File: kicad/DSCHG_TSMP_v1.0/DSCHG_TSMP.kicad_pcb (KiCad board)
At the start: 2 copper layers, 100 x 50 mm, 22 parts, among them J1 TSMP-, J10 R+, J11 R-, J12 Relay_GND, J13 TSAL_TS-, J14 TSAL_TS+, J2 Dis_Relay-, J3 TSMP+, J4 energy meter+, J5 Dis_Relay+, J6 HV-, J7 HV+, J8 SDC+, J9 SDC+&Relay_GND

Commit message: Add files via upload
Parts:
- removed F1: Fuse, Fuse:Fuse_Littelfuse-NANO2-885
- removed J4: energy meter+, Connector_Molex:Molex_Micro-Fit_3.0_43650-0215_1x02_P3.00mm_Vertical
- moved G*** 27.2 mm to (204.5, 96.5)
- moved J2 26.5 mm to (183.0, 77.0)
- moved J3 22.8 mm to (207.0, 77.0), turned to 0 degrees
- moved R1 16.0 mm to (181.0, 90.0), turned to 0 degrees
- moved R2 12.3 mm to (180.9, 99.0)
- moved J9 3.92 mm to (231.0, 77.1)
- moved J8 3.58 mm to (234.0, 113.0)
- moved J13 2.00 mm to (171.0, 77.0)
- moved J5 2.00 mm to (210.0, 112.9)
- moved J6 2.00 mm to (158.0, 90.0)
- moved J7 2.00 mm to (158.0, 102.0)
- moved J10 2.00 mm to (186.0, 112.9)
- moved J11 2.00 mm to (198.0, 112.9)
- moved J14 2.00 mm to (174.0, 112.9)
- moved J1 2.00 mm to (195.0, 77.0)
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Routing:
- net Net-(J13-Pin_1): track 177.7 -> 120.4 mm
- net Net-(J3-Pin_1): track 36.0 -> 87.3 mm
- net Net-(J4-Pin_1): track 36.5 -> 0.00 mm
- net Net-(J1-Pin_1): track 10.9 -> 46.5 mm
- net Net-(J8-Pin_1): track 62.8 -> 77.8 mm
- net Net-(J10-Pin_1): track 125.4 -> 119.1 mm
- net Net-(J12-Pin_1): track 47.5 -> 46.7 mm
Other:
- outline, holes or cut-outs redrawn
- board text removed: "Energy meter+"

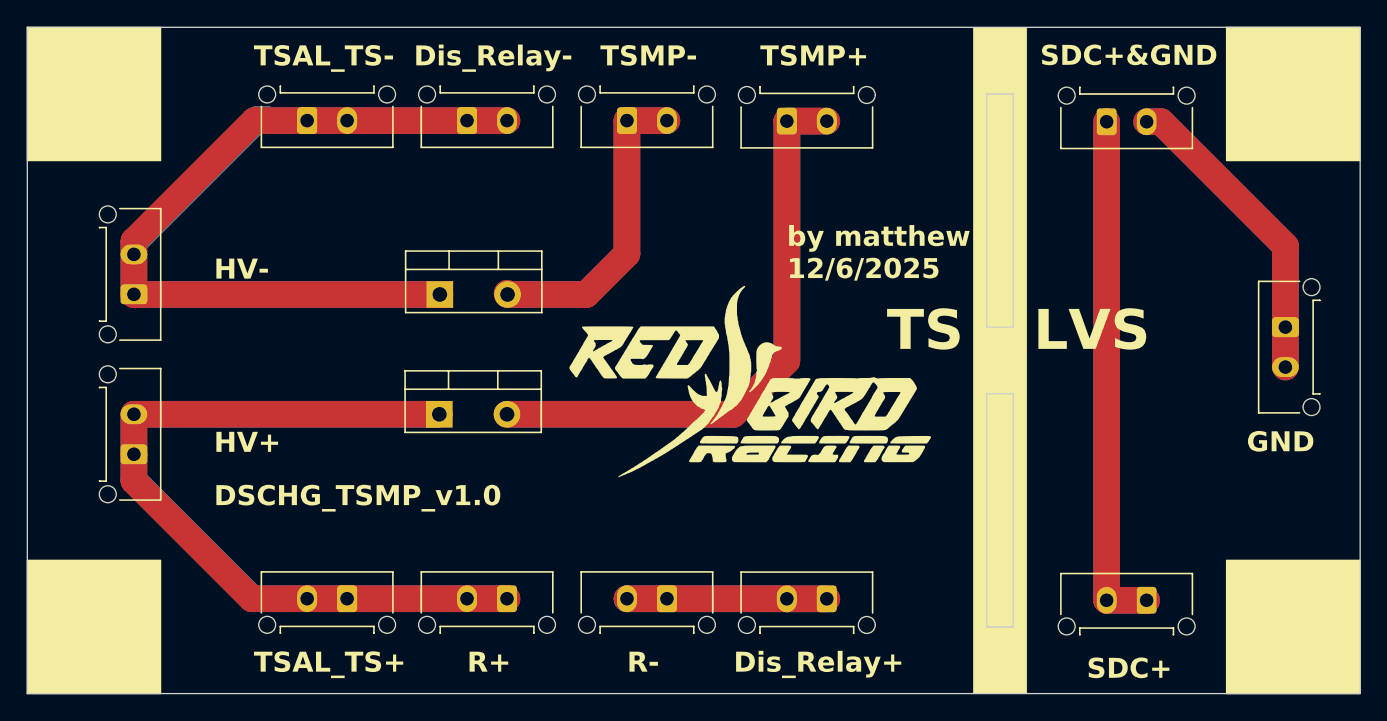
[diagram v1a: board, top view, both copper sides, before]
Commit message: changed some silkscreen
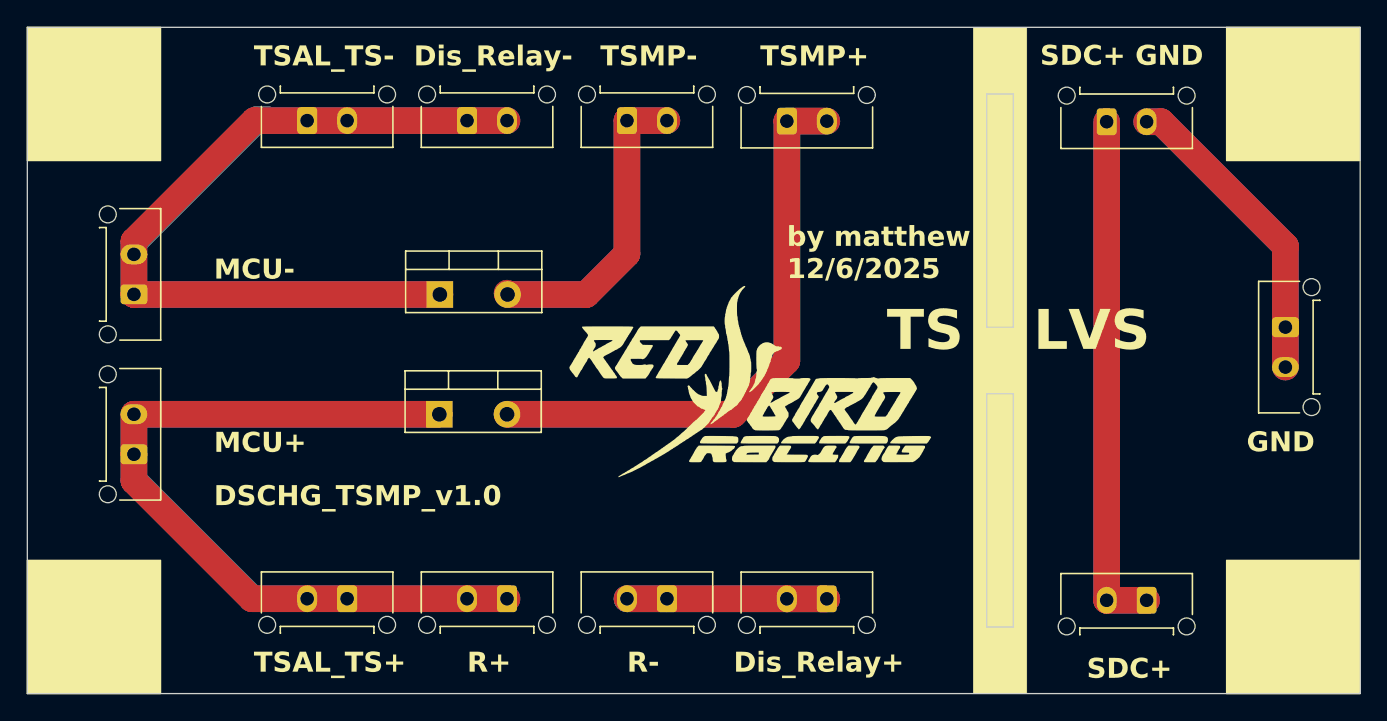
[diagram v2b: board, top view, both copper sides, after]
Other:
- board text added: "MCU+"
- board text added: "MCU-"
- board text added: "SDC+ GND"
- board text removed: "HV+"
- board text removed: "HV-"
- board text removed: "SDC+&GND"
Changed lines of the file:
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@@
 		)
 	)
-	(gr_text "HV+"
+	(gr_text "MCU+\n"
 		(at 164 102.04 0)
 		(layer "F.SilkS")
@@
 		)
 	)
-	(gr_text "SDC+&GND"
+	(gr_text "SDC+ GND"
 		(at 226 73 0)
 		(layer "F.SilkS")
@@
 		)
 	)
-	(gr_text "HV-"
+	(gr_text "MCU-"
 		(at 164 89.04 0)
 		(layer "F.SilkS")
